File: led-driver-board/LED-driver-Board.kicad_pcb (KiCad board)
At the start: 2 copper layers, 80 x 80 mm, 66 parts, among them J1 LED1, J10 LED10, J102 PWR, J103 Dim, J11 LED11, J12 LED12, J13 LED13, J14 LED14, J15 LED15, J16 LED16, J17 LED17, J18 LED18, J19 LED19, J2 LED2, J20 LED20, J21 LED21, J22 LED22, J23 LED23, J24 LED24, J25 LED25, J26 LED26, J27 LED27, J28 LED28, J29 LED29, J3 LED3, J30 LED30, J31 LED31, J32 LED32, J33 JST-XH_02_Pin_vertical, J34 JST-XH_02_Pin_vertical, J35 JST-XH_02_Pin_vertical, J36 JST-XH_02_Pin_vertical, J4 LED4, J5 LED5, J6 LED6, J7 LED7, J8 LED8, J9 LED9, U1 STP08DP05MTR, U2 STP08DP05MTR, U3 STP08DP05MTR, U4 STP08DP05MTR

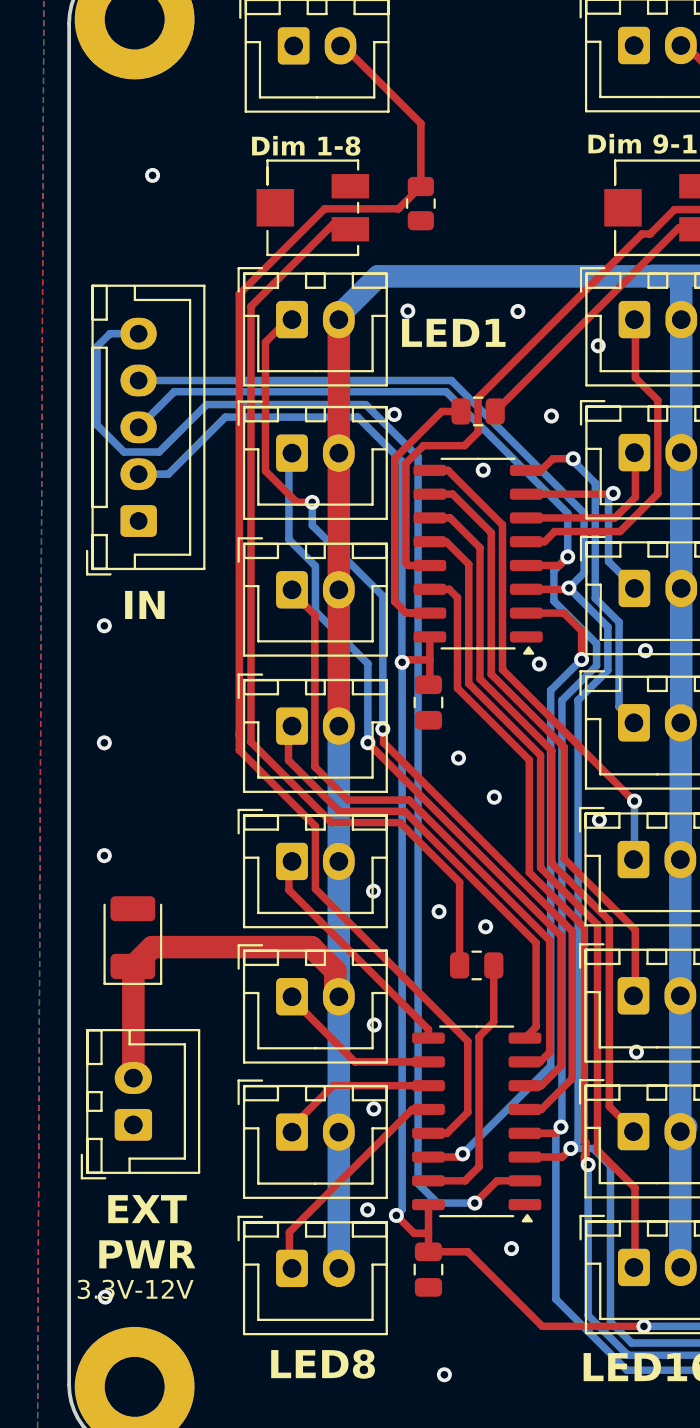
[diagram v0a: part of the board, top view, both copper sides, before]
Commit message: new IN and PWR connector position, update fabrication files
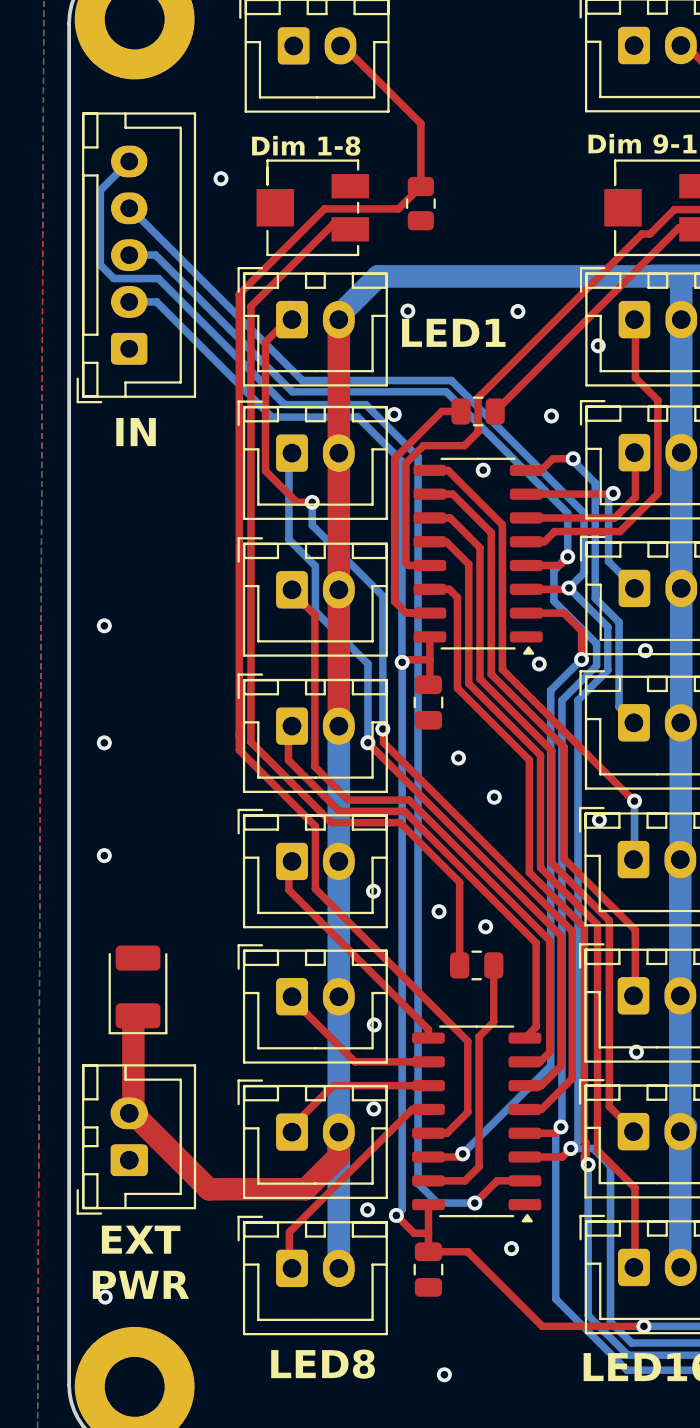
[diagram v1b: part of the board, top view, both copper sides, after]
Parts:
- moved J103 9.21 mm to (73.2, 82.1)
- moved C5 2.65 mm to (73.7, 116.2)
- moved J102 1.90 mm to (73.2, 125.4)
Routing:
- net CLK: track 152.9 -> 157.2 mm
- net LATCH: track 158.6 -> 161.3 mm
- net +5V: track 142.3 -> 144.1 mm
- net VDC: track 288.8 -> 290.1 mm
- net SDI: track 72.1 -> 72.8 mm
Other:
- board text removed: "3.3V-12V"

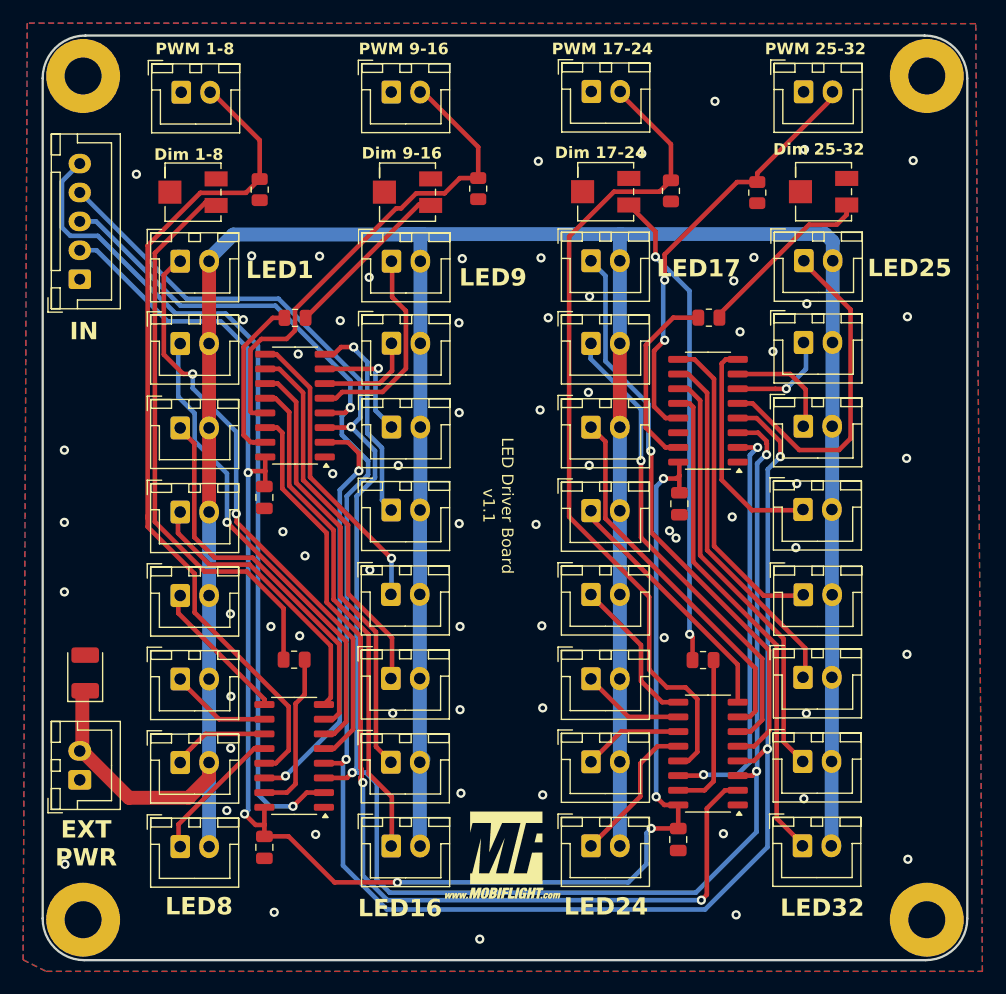
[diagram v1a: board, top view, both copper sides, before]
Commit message: update position of mounting holes, update fabrication files
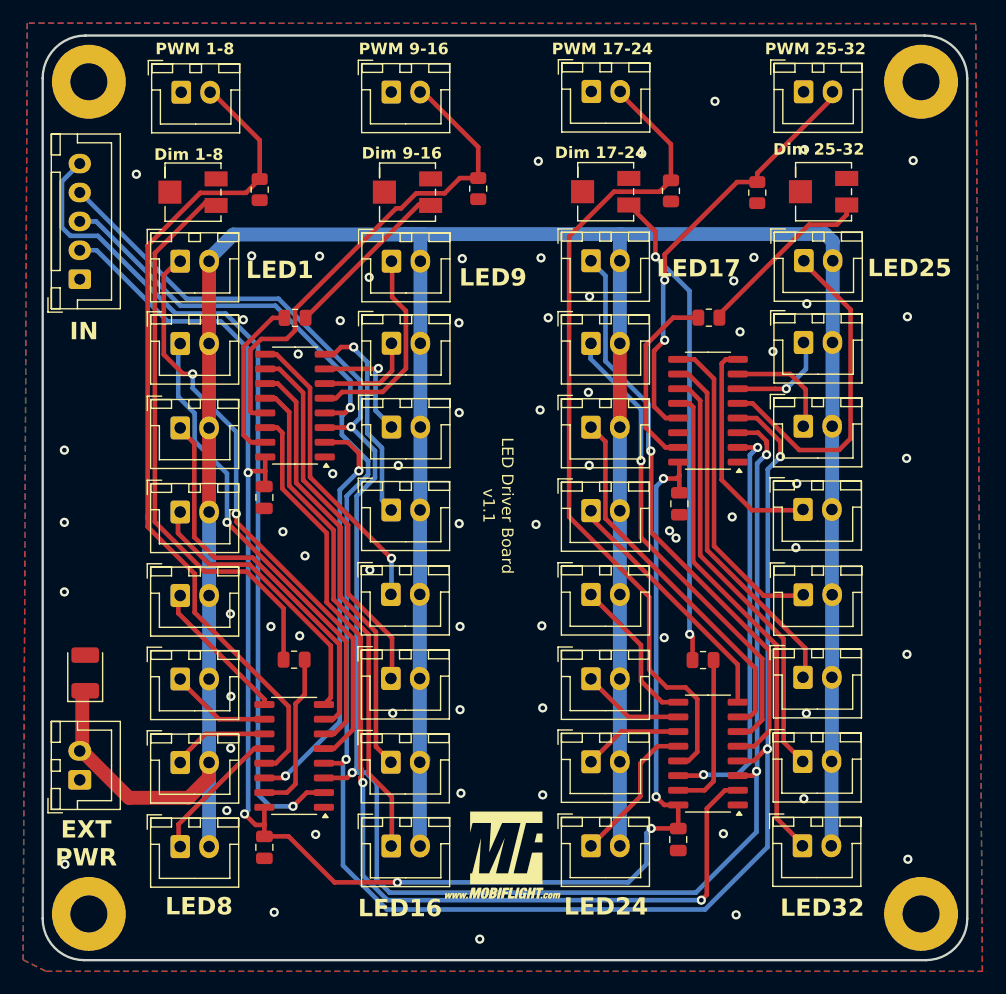
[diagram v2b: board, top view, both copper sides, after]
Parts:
- moved H1 0.71 mm to (74.0, 65.0)
- moved H2 0.71 mm to (146.0, 65.0)
- moved H3 0.71 mm to (74.0, 137.0)
- moved H4 0.71 mm to (146.0, 137.0)
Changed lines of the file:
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@@
 		(locked yes)
 		(layer "F.Cu")
-		(at 73.5 64.5)
+		(at 74 65)
 		(descr "Mounting Hole 3.2mm, M3")
 		(tags "mounting hole 3.2mm m3")
@@
 		(locked yes)
 		(layer "F.Cu")
-		(at 73.5 137.5)
+		(at 74 137)
 		(descr "Mounting Hole 3.2mm, M3")
 		(tags "mounting hole 3.2mm m3")
@@
 		(locked yes)
 		(layer "F.Cu")
-		(at 146.5 137.5)
+		(at 146 137)
 		(descr "Mounting Hole 3.2mm, M3")
 		(tags "mounting hole 3.2mm m3")
@@
 		(locked yes)
 		(layer "F.Cu")
-		(at 146.5 64.5)
+		(at 146 65)
 		(descr "Mounting Hole 3.2mm, M3")
 		(tags "mounting hole 3.2mm m3")
